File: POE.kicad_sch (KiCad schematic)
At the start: 35 parts, among them J3 7466003R, J5 7466003R, Q1 FDS2582, T1 PA2369NL, U13 VO615A, U14 TL431PK, U3 NCP1081

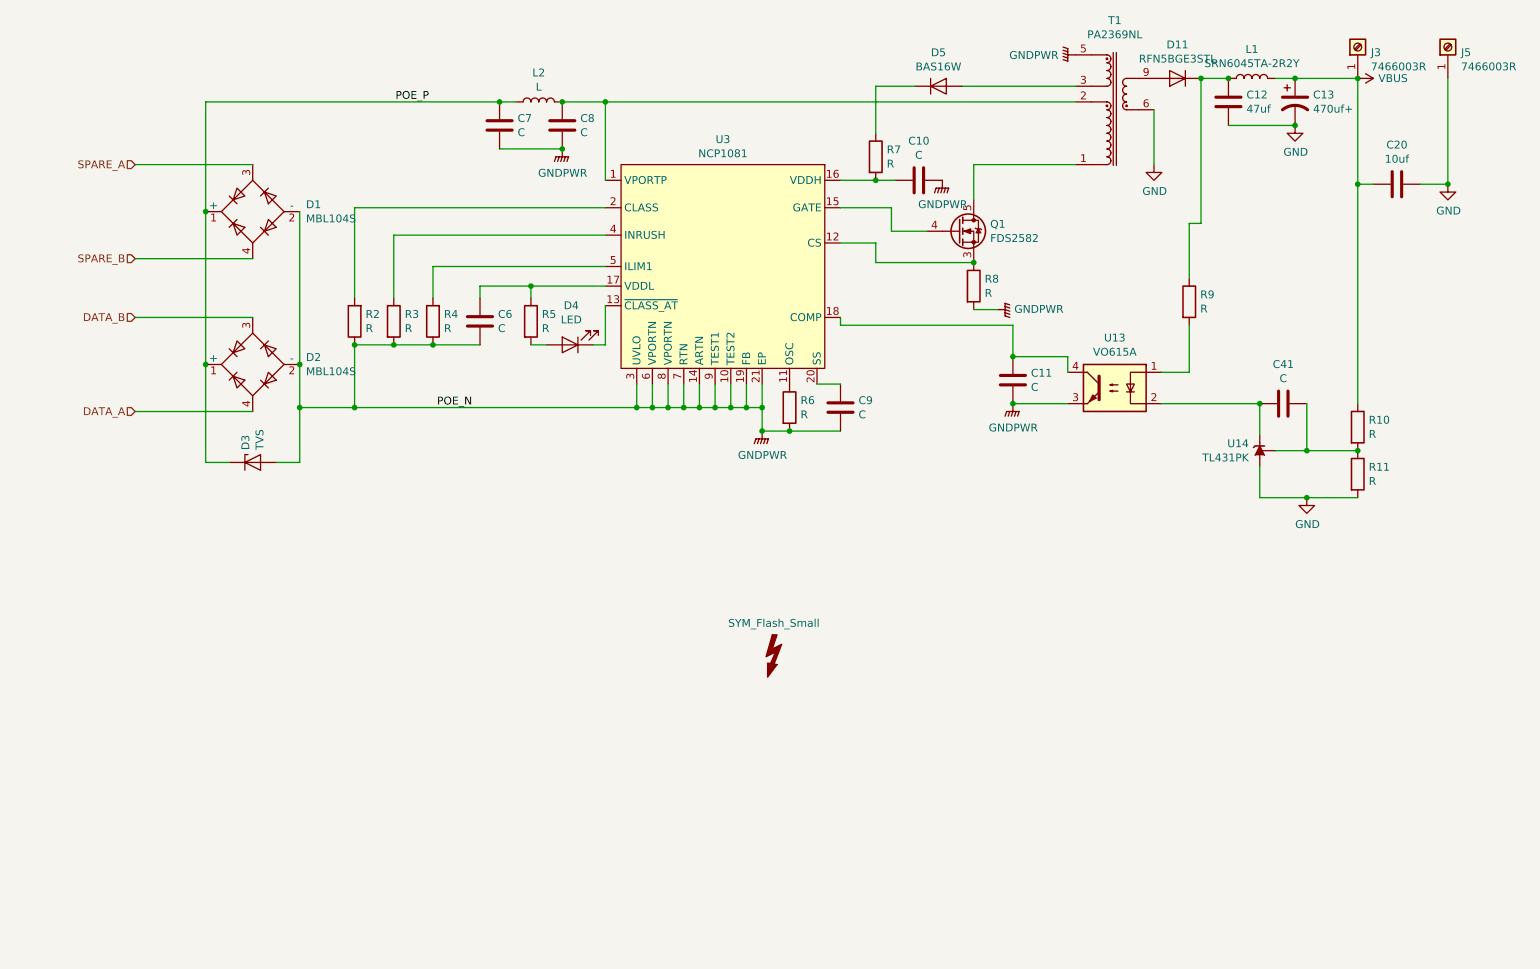
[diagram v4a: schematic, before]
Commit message: Add missing detection resistor
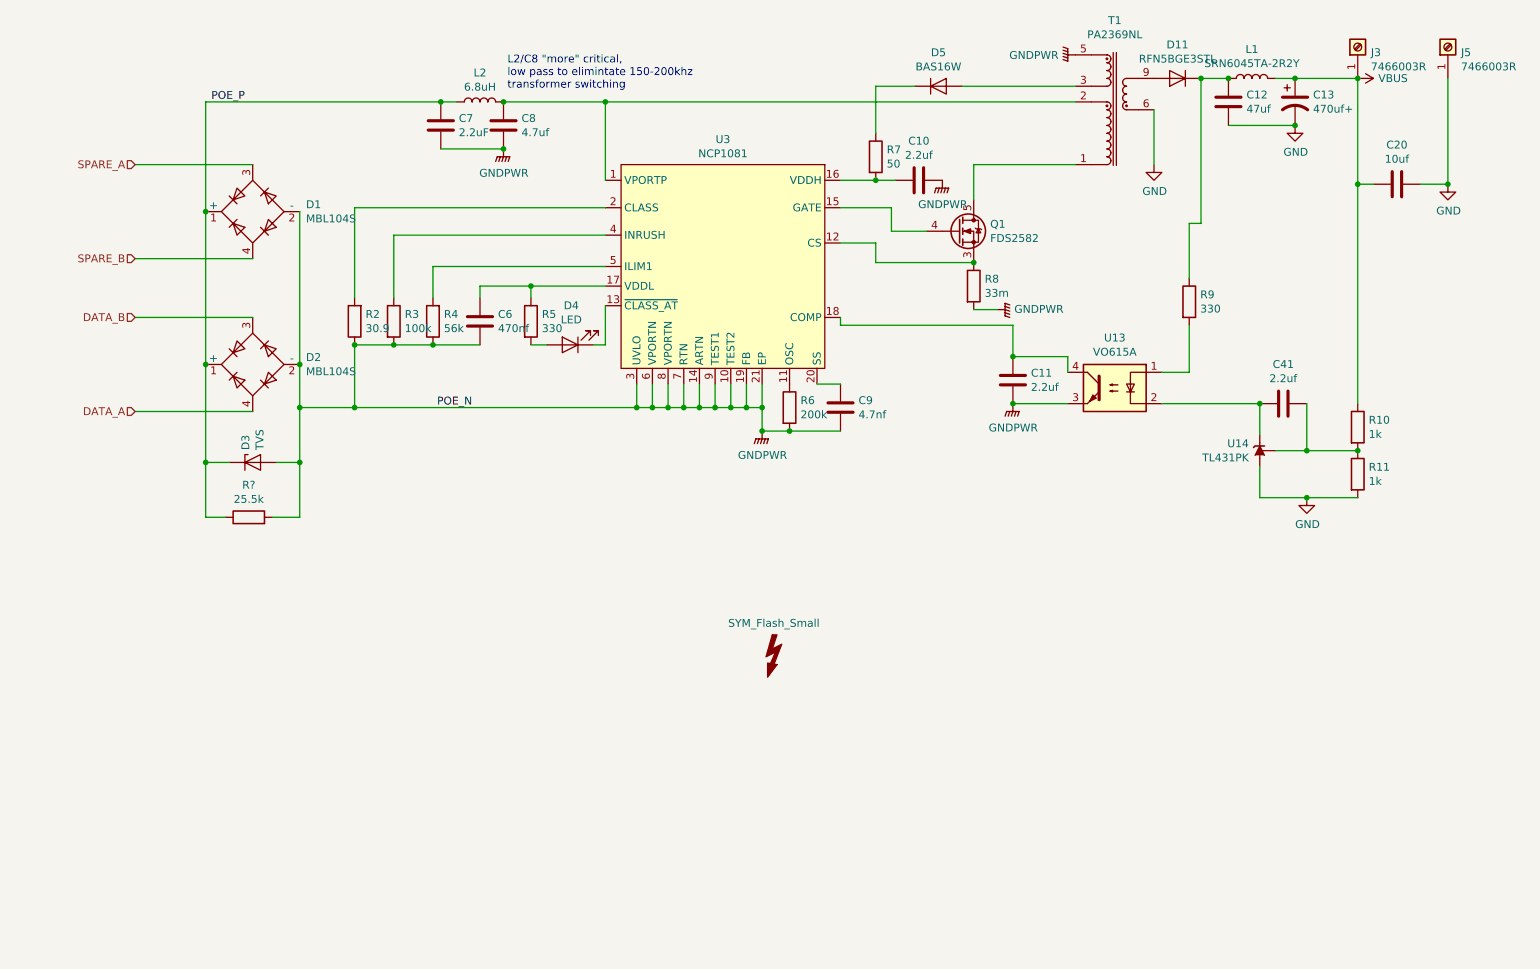
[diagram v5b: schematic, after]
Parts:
- added R?: 25.5k, Resistor_SMD:R_0805_2012Metric, symbol Device:R
- C10, C11, C41: value C -> 2.2uf
- C6: value C -> 470nf
- C7: value C -> 2.2uF
- C8: value C -> 4.7uf
- C9: value C -> 4.7nf
- L2: value L -> 6.8uH
- R10, R11: value R -> 1k
- R2: value R -> 30.9
- R3: value R -> 100k
- R4: value R -> 56k
- R5, R9: value R -> 330
- R6: value R -> 200k
- R7: value R -> 50
- R8: value R -> 33m
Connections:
- net GNDPWR: now also R?.2
- net POE_P: now also R?.1
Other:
- note added: "L2/C8 "more" critical, low pass to elimintate 150-200khz transformer switching"
- moved on the sheet: C7, C8, L2

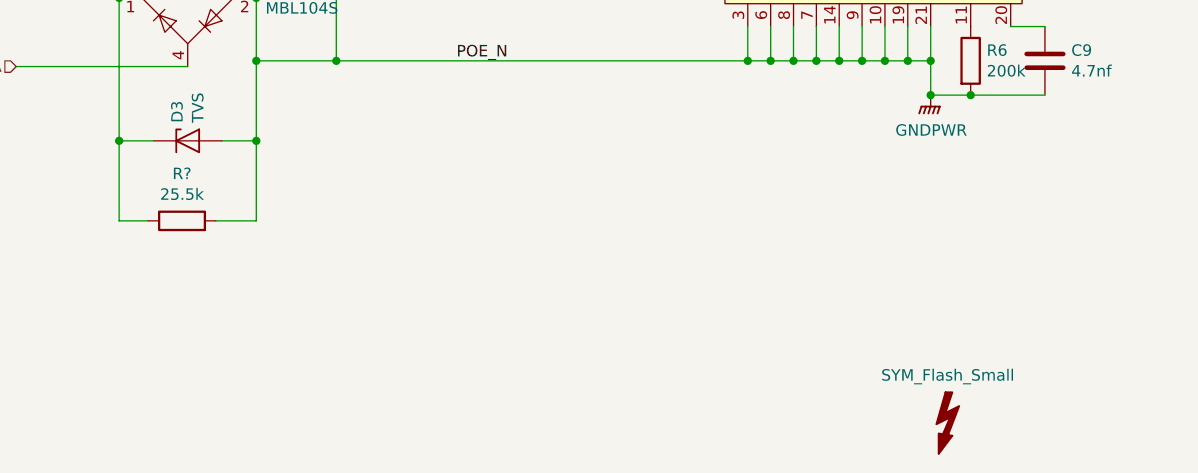
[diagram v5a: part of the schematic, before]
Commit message: More routing cleanup
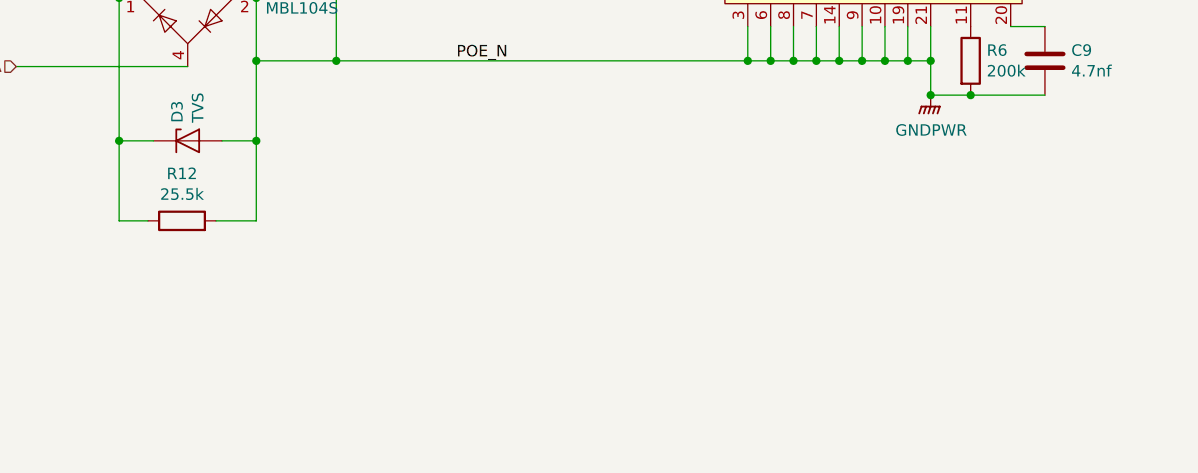
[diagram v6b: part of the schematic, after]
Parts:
- U13: footprint Package_SO:SO-4_4.4x3.9mm_P2.54mm -> hub75_poe:VO615A-9X017T
- gave numbers to parts that had none: 1
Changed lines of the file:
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@@
-(kicad_sch (version 20200608) (host eeschema "5.99.0-unknown-e164269~101~ubuntu20.04.1")
+(kicad_sch (version 20200618) (host eeschema "5.99.0-unknown-b48a627~101~ubuntu20.04.1")
   (page 4 7)
   (paper "A4")
@@
     (rev "TEST")
   )
-  (junction (at 52.07 61.595))
-  (junction (at 52.07 86.36))
-  (junction (at 52.07 102.235))
-  (junction (at 67.31 86.36))
-  (junction (at 67.31 93.345))
-  (junction (at 67.31 102.235))
-  (junction (at 76.2 83.185))
-  (junction (at 76.2 93.345))
-  (junction (at 82.55 83.185))
-  (junction (at 88.9 83.185))
-  (junction (at 90.17 43.815))
-  (junction (at 100.33 43.815))
-  (junction (at 100.33 51.435))
-  (junction (at 104.775 73.66))
-  (junction (at 116.84 43.815))
-  (junction (at 121.92 93.345))
-  (junction (at 124.46 93.345))
-  (junction (at 127 93.345))
-  (junction (at 129.54 93.345))
-  (junction (at 132.08 93.345))
-  (junction (at 134.62 93.345))
-  (junction (at 137.16 93.345))
-  (junction (at 139.7 93.345))
-  (junction (at 142.24 93.345))
-  (junction (at 142.24 97.155))
-  (junction (at 146.685 97.155))
-  (junction (at 160.655 56.515))
-  (junction (at 176.53 69.85))
-  (junction (at 182.88 85.09))
-  (junction (at 182.88 92.71))
-  (junction (at 213.36 40.005))
-  (junction (at 217.805 40.005))
-  (junction (at 222.885 92.71))
-  (junction (at 228.6 40.005))
-  (junction (at 228.6 47.625))
-  (junction (at 230.505 100.33))
-  (junction (at 230.505 107.95))
-  (junction (at 238.76 40.005))
-  (junction (at 238.76 57.15))
-  (junction (at 238.76 100.33))
-  (junction (at 253.365 57.15))
+  (junction (at 52.07 61.595) (diameter 0) (color 0 0 0 0))
+  (junction (at 52.07 86.36) (diameter 0) (color 0 0 0 0))
+  (junction (at 52.07 102.235) (diameter 0) (color 0 0 0 0))
+  (junction (at 67.31 86.36) (diameter 0) (color 0 0 0 0))
+  (junction (at 67.31 93.345) (diameter 0) (color 0 0 0 0))
+  (junction (at 67.31 102.235) (diameter 0) (color 0 0 0 0))
+  (junction (at 76.2 83.185) (diameter 0) (color 0 0 0 0))
+  (junction (at 76.2 93.345) (diameter 0) (color 0 0 0 0))
+  (junction (at 82.55 83.185) (diameter 0) (color 0 0 0 0))
+  (junction (at 88.9 83.185) (diameter 0) (color 0 0 0 0))
+  (junction (at 90.17 43.815) (diameter 0) (color 0 0 0 0))
+  (junction (at 100.33 43.815) (diameter 0) (color 0 0 0 0))
+  (junction (at 100.33 51.435) (diameter 0) (color 0 0 0 0))
+  (junction (at 104.775 73.66) (diameter 0) (color 0 0 0 0))
+  (junction (at 116.84 43.815) (diameter 0) (color 0 0 0 0))
+  (junction (at 121.92 93.345) (diameter 0) (color 0 0 0 0))
+  (junction (at 124.46 93.345) (diameter 0) (color 0 0 0 0))
+  (junction (at 127 93.345) (diameter 0) (color 0 0 0 0))
+  (junction (at 129.54 93.345) (diameter 0) (color 0 0 0 0))
+  (junction (at 132.08 93.345) (diameter 0) (color 0 0 0 0))
+  (junction (at 134.62 93.345) (diameter 0) (color 0 0 0 0))
+  (junction (at 137.16 93.345) (diameter 0) (color 0 0 0 0))
+  (junction (at 139.7 93.345) (diameter 0) (color 0 0 0 0))
+  (junction (at 142.24 93.345) (diameter 0) (color 0 0 0 0))
+  (junction (at 142.24 97.155) (diameter 0) (color 0 0 0 0))
+  (junction (at 146.685 97.155) (diameter 0) (color 0 0 0 0))
+  (junction (at 160.655 56.515) (diameter 0) (color 0 0 0 0))
+  (junction (at 176.53 69.85) (diameter 0) (color 0 0 0 0))
+  (junction (at 182.88 85.09) (diameter 0) (color 0 0 0 0))
+  (junction (at 182.88 92.71) (diameter 0) (color 0 0 0 0))
+  (junction (at 213.36 40.005) (diameter 0) (color 0 0 0 0))
+  (junction (at 217.805 40.005) (diameter 0) (color 0 0 0 0))
+  (junction (at 222.885 92.71) (diameter 0) (color 0 0 0 0))
+  (junction (at 228.6 40.005) (diameter 0) (color 0 0 0 0))
+  (junction (at 228.6 47.625) (diameter 0) (color 0 0 0 0))
+  (junction (at 230.505 100.33) (diameter 0) (color 0 0 0 0))
+  (junction (at 230.505 107.95) (diameter 0) (color 0 0 0 0))
+  (junction (at 238.76 40.005) (diameter 0) (color 0 0 0 0))
+  (junction (at 238.76 57.15) (diameter 0) (color 0 0 0 0))
+  (junction (at 238.76 100.33) (diameter 0) (color 0 0 0 0))
+  (junction (at 253.365 57.15) (diameter 0) (color 0 0 0 0))
   (wire (pts (xy 40.64 53.975) (xy 59.69 53.975))
     (stroke (width 0) (type solid) (color 0 0 0 0))
@@
   (symbol (lib_id "Device:R") (at 59.055 111.125 90) (unit 1)
     (in_bom yes) (on_board yes)
-    (property "Reference" "R?" (id 0) (at 59.055 105.8988 90))
+    (property "Reference" "R12" (id 0) (at 59.055 105.8988 90))
     (property "Value" "25.5k" (id 1) (at 59.055 108.1975 90))
     (property "Footprint" "Resistor_SMD:R_0805_2012Metric" (id 2) (at 59.055 112.903 90)
@@
     )
     (property "Datasheet" "~" (id 3) (at 238.76 104.14 0)
-      (effects (font (size 1.27 1.27)) hide)
-    )
-  )
-  (symbol (lib_id "Graphic:SYM_Flash_Small") (at 144.145 133.985 0) (unit 1)
-    (in_bom yes) (on_board yes)
-    (property "Reference" "#SYM1" (id 0) (at 141.859 133.985 90)
-      (effects (font (size 1.27 1.27)) hide)
-    )
-    (property "Value" "SYM_Flash_Small" (id 1) (at 144.145 128.289 0))
-    (property "Footprint" "Symbol:Symbol_Highvoltage_Type1_CopperTop_Small" (id 2) (at 144.145 134.62 0)
-      (effects (font (size 1.27 1.27)) hide)
-    )
-    (property "Datasheet" "~" (id 3) (at 154.305 136.525 0)
       (effects (font (size 1.27 1.27)) hide)
     )
@@
     (property "Reference" "U13" (id 0) (at 199.39 82.0482 0))
     (property "Value" "VO615A" (id 1) (at 199.39 84.3469 0))
-    (property "Footprint" "Package_SO:SO-4_4.4x3.9mm_P2.54mm" (id 2) (at 199.39 90.17 0)
-      (effects (font (size 1.27 1.27)) hide)
-    )
+    (property "Footprint" "hub75_poe:VO615A-9X017T" (id 2) (at 199.39 90.17 0)
+      (effects (font (size 1.27 1.27)) hide)
+    )

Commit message: Fix SOT-89-3 footprint
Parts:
- U14: footprint Package_TO_SOT_SMD:SOT-89-3 -> hub75_poe:SOT-89-3
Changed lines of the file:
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@@
-(kicad_sch (version 20200618) (host eeschema "5.99.0-unknown-b48a627~101~ubuntu20.04.1")
+(kicad_sch (version 20200618) (host eeschema "5.99.0-unknown-19b7755~101~ubuntu20.04.1")
   (page 4 7)
   (paper "A4")
@@
       (effects (font (size 1.27 1.27)) (justify right))
     )
-    (property "Footprint" "Package_TO_SOT_SMD:SOT-89-3" (id 2) (at 219.075 100.33 0)
+    (property "Footprint" "hub75_poe:SOT-89-3" (id 2) (at 219.075 100.33 0)
       (effects (font (size 1.27 1.27) italic) hide)
     )
